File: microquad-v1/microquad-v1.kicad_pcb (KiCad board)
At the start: 2 copper layers, 53.3 x 53.3 mm, 79 parts, among them J1 USB_microB_2040002-1, M1 Motor_DC, M2 Motor_DC, M3 Motor_DC, M4 Motor_DC, M5 Motor_DC, M6 Motor_DC, Q1 Q_NMOS_GSD, Q2 Q_NMOS_GSD, Q3 Q_NMOS_GSD, Q4 Q_NMOS_GSD, Q5 Q_NMOS_GSD, Q6 Q_NMOS_GSD, SW1 SERIAL, SW2 POWER, SW3 RESET, U1 ATMEGA328PB, U2 MCP1703A-3302_SOT23, U3 FT230XS, U4 MCP73812T, U5 MAX6333UR18D3

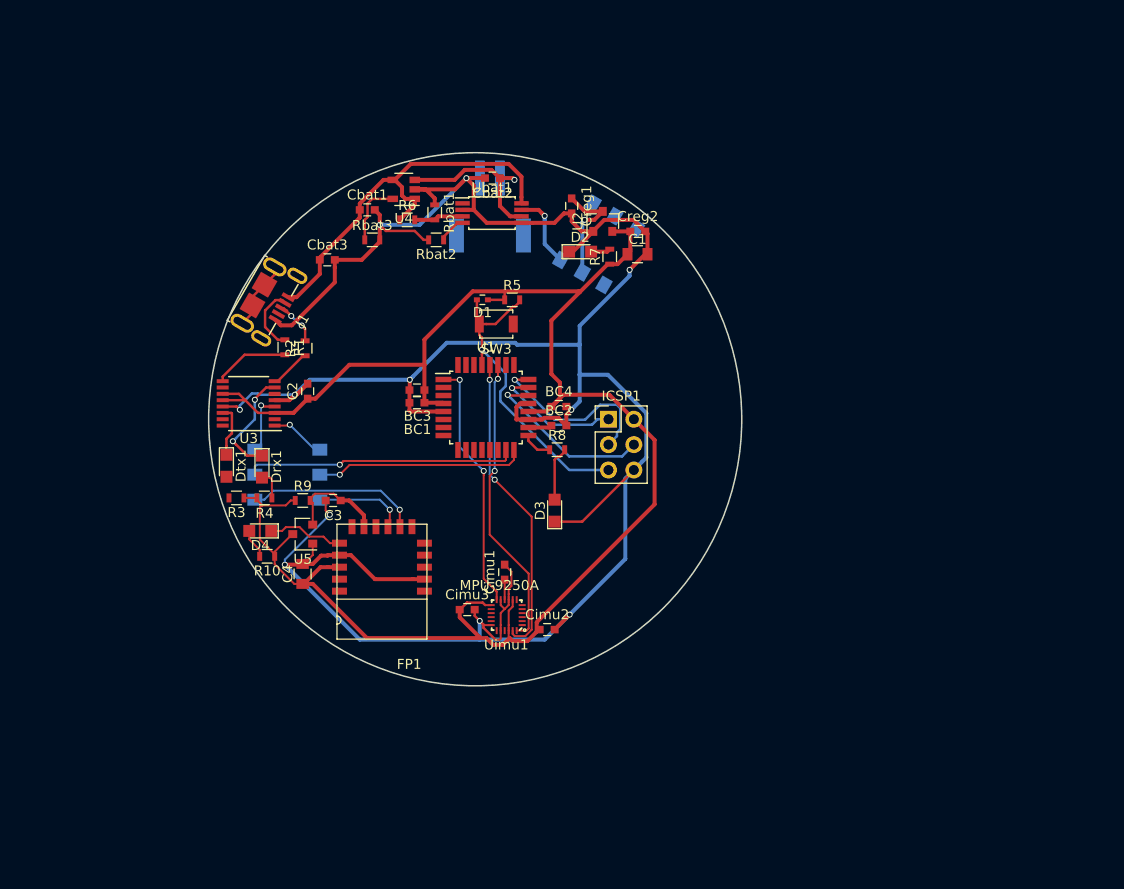
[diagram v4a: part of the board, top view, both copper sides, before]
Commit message: Added ground pour
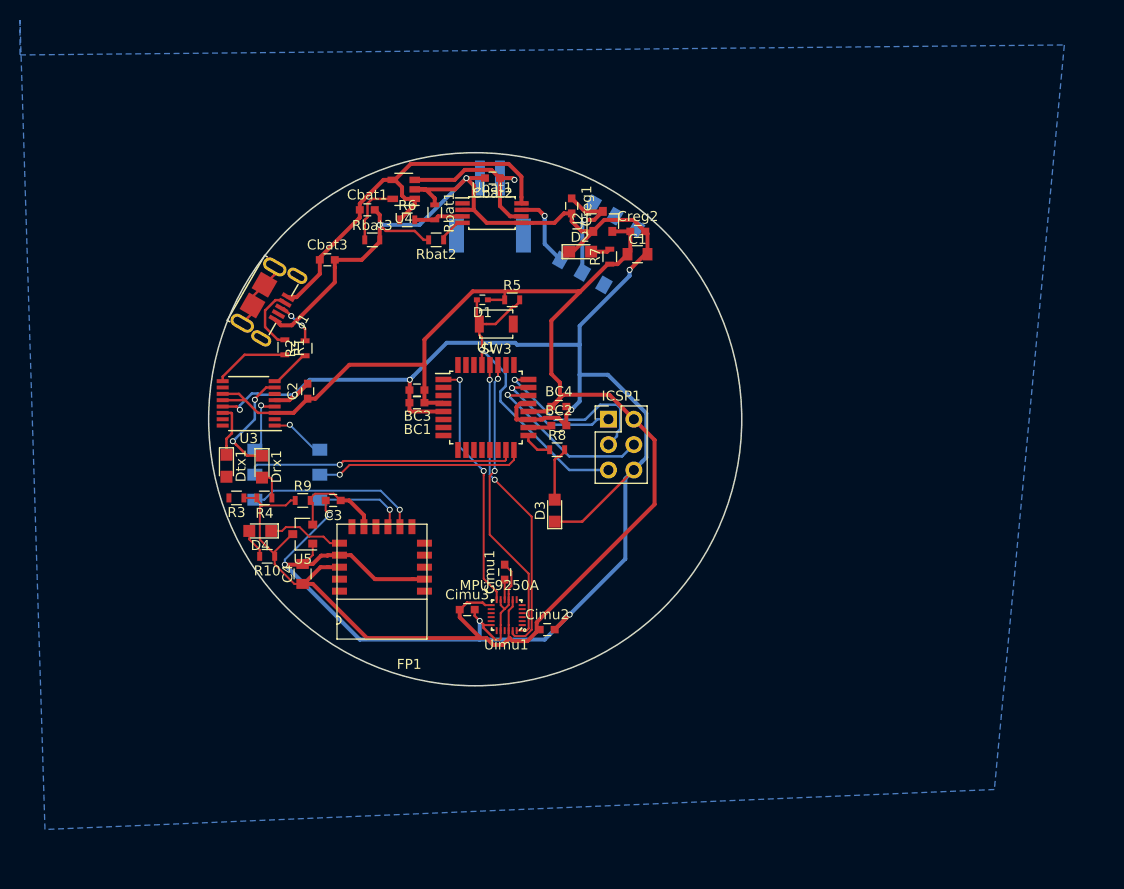
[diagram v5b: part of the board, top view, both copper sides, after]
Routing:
- added copper zone on B.Cu, net GND
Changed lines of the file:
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@@
   (segment (start 149.781073 104.775) (end 149.730288 104.825785) (width 0.25) (layer F.Cu) (net 31))
   (segment (start 150 104) (end 151.35 104) (width 0.25) (layer F.Cu) (net 32))
+  (segment (start 160.234999 109.640001) (end 160.234999 109.265001) (width 0.25) (layer B.Cu) (net 32))
+  (segment (start 159.385 110.49) (end 160.234999 109.640001) (width 0.25) (layer B.Cu) (net 32))
+  (segment (start 160.560001 106.839999) (end 160.220002 106.5) (width 0.25) (layer B.Cu) (net 32))
+  (segment (start 160.560001 108.939999) (end 160.560001 106.839999) (width 0.25) (layer B.Cu) (net 32))
+  (segment (start 160.234999 109.265001) (end 160.560001 108.939999) (width 0.25) (layer B.Cu) (net 32))
+  (segment (start 158.549998 106.5) (end 157.049998 108) (width 0.25) (layer B.Cu) (net 32))
+  (segment (start 160.220002 106.5) (end 158.549998 106.5) (width 0.25) (layer B.Cu) (net 32))
+  (via (at 150 104) (size 0.6) (drill 0.4) (layers F.Cu B.Cu) (net 32))
+  (segment (start 154 108) (end 150 104) (width 0.25) (layer B.Cu) (net 32))
+  (segment (start 157.049998 108) (end 154 108) (width 0.25) (layer B.Cu) (net 32))
   (segment (start 151.35 104) (end 151.375 103.975) (width 0.25) (layer F.Cu) (net 32))
-  (segment (start 157.049998 108) (end 154 108) (width 0.25) (layer B.Cu) (net 32))
-  (segment (start 154 108) (end 150 104) (width 0.25) (layer B.Cu) (net 32))
-  (via (at 150 104) (size 0.6) (drill 0.4) (layers F.Cu B.Cu) (net 32))
-  (segment (start 160.220002 106.5) (end 158.549998 106.5) (width 0.25) (layer B.Cu) (net 32))
-  (segment (start 158.549998 106.5) (end 157.049998 108) (width 0.25) (layer B.Cu) (net 32))
-  (segment (start 160.234999 109.265001) (end 160.560001 108.939999) (width 0.25) (layer B.Cu) (net 32))
-  (segment (start 160.560001 108.939999) (end 160.560001 106.839999) (width 0.25) (layer B.Cu) (net 32))
-  (segment (start 160.560001 106.839999) (end 160.220002 106.5) (width 0.25) (layer B.Cu) (net 32))
-  (segment (start 159.385 110.49) (end 160.234999 109.640001) (width 0.25) (layer B.Cu) (net 32))
-  (segment (start 160.234999 109.640001) (end 160.234999 109.265001) (width 0.25) (layer B.Cu) (net 32))
   (segment (start 161.925 110.49) (end 160.749999 111.665001) (width 0.25) (layer B.Cu) (net 33))
   (segment (start 149.364143 105.575) (end 149.296792 105.507649) (width 0.25) (layer F.Cu) (net 33))
@@
   (segment (start 151.700012 129.014269) (end 151.700012 127.799988) (width 0.2) (layer F.Cu) (net 55))
   (segment (start 149.8 129.1) (end 149.8 129.442881) (width 0.2) (layer F.Cu) (net 55))
+  (zone (net 1) (net_name GND) (layer B.Cu) (hatch edge 0.508)
+    (connect_pads (clearance 0.508))
+    (min_thickness 0.254)
+    (fill yes (arc_segments 16) (thermal_gap 0.508) (thermal_bridge_width 0.508))
+    (polygon
+      (pts
+        (xy 100.5 71.5) (xy 205 70.5) (xy 198 145) (xy 103 149) (xy 100.5 68)
+      )
+    )
+  )
 )

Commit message: Made a pretty array of motors
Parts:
- added C10: 10uF, Capacitors_SMD:C_0805, F.Cu at (225.3, 72.6)
- added C10: 10uF, Capacitors_SMD:C_0805, F.Cu at (250.7, 68.8)
- added C10: 10uF, Capacitors_SMD:C_0805, F.Cu at (266.7, 88.9)
- added C10: 10uF, Capacitors_SMD:C_0805, F.Cu at (257.3, 112.8)
- added C10: 10uF, Capacitors_SMD:C_0805, F.Cu at (231.9, 116.6)
- added D15: BAS521LP-7, Diodes_SMD:D_SOD-123F, F.Cu at (226.7, 67.4)
- added D15: BAS521LP-7, Diodes_SMD:D_SOD-123F, F.Cu at (255.9, 67.4)
- added D15: BAS521LP-7, Diodes_SMD:D_SOD-123F, F.Cu at (270.5, 92.7)
- added D15: BAS521LP-7, Diodes_SMD:D_SOD-123F, F.Cu at (255.9, 118.0)
- added D15: BAS521LP-7, Diodes_SMD:D_SOD-123F, F.Cu at (226.7, 118.0)
- added D16: DNP, Diodes_SMD:D_2114, F.Cu at (230.3, 71.2)
- added D16: DNP, Diodes_SMD:D_2114, F.Cu at (254.5, 72.4)
- added D16: DNP, Diodes_SMD:D_2114, F.Cu at (265.4, 94.0)
- added D16: DNP, Diodes_SMD:D_2114, F.Cu at (252.3, 114.2)
- added D16: DNP, Diodes_SMD:D_2114, F.Cu at (228.1, 113.0)
- added M6: Motor_DC, motor:quad_motor_v1, F.Cu at (223.5, 61.9)
- added M6: Motor_DC, motor:quad_motor_v1, F.Cu at (259.1, 61.9)
- added M6: Motor_DC, motor:quad_motor_v1, F.Cu at (276.9, 92.7)
- added M6: Motor_DC, motor:quad_motor_v1, F.Cu at (259.1, 123.5)
- added M6: Motor_DC, motor:quad_motor_v1, F.Cu at (223.5, 123.5)
- added Q6: Q_NMOS_GSD, TO_SOT_Packages_SMD:SOT-23, F.Cu at (231.8, 76.2)
- added Q6: Q_NMOS_GSD, TO_SOT_Packages_SMD:SOT-23, F.Cu at (250.8, 76.2)
- added Q6: Q_NMOS_GSD, TO_SOT_Packages_SMD:SOT-23, F.Cu at (260.4, 92.7)
- added Q6: Q_NMOS_GSD, TO_SOT_Packages_SMD:SOT-23, F.Cu at (250.8, 109.2)
- added Q6: Q_NMOS_GSD, TO_SOT_Packages_SMD:SOT-23, F.Cu at (231.8, 109.2)
- moved D15 105.0 mm to (212.1, 92.7), turned to 90 degrees
- moved M6 102.3 mm to (205.7, 92.7), turned to 90 degrees
- moved C10 101.5 mm to (215.9, 96.5)
- moved D16 100.3 mm to (217.2, 91.4), turned to 270 degrees
- moved Q6 98.5 mm to (222.2, 92.7)

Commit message: Fixed motor component labels and reimported netlist
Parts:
- removed the C5 at (135.0, 203.2)
- removed the C6 at (148.8, 227.6)
- removed the C7 at (186.3, 197.5)
- removed the C8 at (224.4, 223.6)
- removed the C9 at (186.7, 223.0)
- removed the D10 at (188.2, 191.2)
- removed the D11 at (217.3, 223.5)
- removed the D12 at (226.3, 217.3)
- removed the D13 at (179.7, 222.9)
- removed the D14 at (188.6, 216.6)
- removed the D5 at (128.0, 203.6)
- removed the D6 at (143.4, 198.2)
- removed the D7 at (141.7, 227.5)
- removed the D8 at (150.6, 221.2)
- removed the D9 at (179.2, 197.4)
- removed the M1 at (132.1, 194.1)
- removed the M2 at (130.1, 224.9)
- removed the M3 at (167.6, 194.8)
- removed the M4 at (205.7, 220.9)
- removed the M5 at (168.0, 220.3)
- removed the Q1 at (144.6, 191.0)
- removed the Q2 at (141.8, 221.0)
- removed the Q3 at (179.3, 191.0)
- removed the Q4 at (217.4, 217.1)
- removed the Q5 at (179.7, 216.4)
- renumbered C10 to C5, C10 to C6, C10 to C7, C10 to C8, C10 to C9, D16 to D10, D15 to D11, D16 to D12, D15 to D13, D16 to D14, D15 to D5, D16 to D6, D15 to D7, D16 to D8, D15 to D9, M6 to M1, M6 to M2, M6 to M3, M6 to M4, M6 to M5, Q6 to Q1, Q6 to Q2, Q6 to Q3, Q6 to Q4, Q6 to Q5
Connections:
- C5 pad 2: /Motor6/VBAT -> /Motor1/VBAT
- C6 pad 2: /Motor6/VBAT -> /Motor2/VBAT
- C7 pad 2: /Motor6/VBAT -> /Motor3/VBAT
- C8 pad 2: /Motor6/VBAT -> /Motor4/VBAT
- C9 pad 2: /Motor6/VBAT -> /Motor5/VBAT
- D10 pad 1: Net-(D15-Pad2) -> Net-(D10-Pad1)
- D11 pad 1: /Motor6/VBAT -> /Motor4/VBAT
- D11 pad 2: Net-(D15-Pad2) -> Net-(D11-Pad2)
- D12 pad 1: Net-(D15-Pad2) -> Net-(D11-Pad2)
- D13 pad 1: /Motor6/VBAT -> /Motor5/VBAT
- D13 pad 2: Net-(D15-Pad2) -> Net-(D13-Pad2)
- D14 pad 1: Net-(D15-Pad2) -> Net-(D13-Pad2)
- D5 pad 1: /Motor6/VBAT -> /Motor1/VBAT
- D5 pad 2: Net-(D15-Pad2) -> Net-(D5-Pad2)
- D6 pad 1: Net-(D15-Pad2) -> Net-(D5-Pad2)
- D7 pad 1: /Motor6/VBAT -> /Motor2/VBAT
- D7 pad 2: Net-(D15-Pad2) -> Net-(D7-Pad2)
- D8 pad 1: Net-(D15-Pad2) -> Net-(D7-Pad2)
- D9 pad 1: /Motor6/VBAT -> /Motor3/VBAT
- D9 pad 2: Net-(D15-Pad2) -> Net-(D10-Pad1)
- FP1 pad 1: (no net) -> Net-(FP1-Pad1)
- FP1 pad 11: (no net) -> Net-(FP1-Pad11)
- FP1 pad 15: (no net) -> Net-(FP1-Pad15)
- FP1 pad 16: (no net) -> Net-(FP1-Pad16)
- FP1 pad 3: (no net) -> Net-(FP1-Pad3)
- FP1 pad 4: (no net) -> Net-(FP1-Pad4)
- FP1 pad 5: (no net) -> Net-(FP1-Pad5)
- FP1 pad 6: (no net) -> Net-(FP1-Pad6)
- FP1 pad 9: (no net) -> Net-(FP1-Pad9)
- J1 pad 4: (no net) -> Net-(J1-Pad4)
- M1 pad 1: /Motor6/VBAT -> /Motor1/VBAT
- M1 pad 2: Net-(D15-Pad2) -> Net-(D5-Pad2)
- M2 pad 1: /Motor6/VBAT -> /Motor2/VBAT
- M2 pad 2: Net-(D15-Pad2) -> Net-(D7-Pad2)
- M3 pad 1: /Motor6/VBAT -> /Motor3/VBAT
- M3 pad 2: Net-(D15-Pad2) -> Net-(D10-Pad1)
- M4 pad 1: /Motor6/VBAT -> /Motor4/VBAT
- M4 pad 2: Net-(D15-Pad2) -> Net-(D11-Pad2)
- M5 pad 1: /Motor6/VBAT -> /Motor5/VBAT
- M5 pad 2: Net-(D15-Pad2) -> Net-(D13-Pad2)
- Q1 pad 1: /Motor6/ENABLE -> /Motor1/ENABLE
- Q1 pad 3: Net-(D15-Pad2) -> Net-(D5-Pad2)
- Q2 pad 1: /Motor6/ENABLE -> /Motor2/ENABLE
- Q2 pad 3: Net-(D15-Pad2) -> Net-(D7-Pad2)
- Q3 pad 1: /Motor6/ENABLE -> /Motor3/ENABLE
- Q3 pad 3: Net-(D15-Pad2) -> Net-(D10-Pad1)
- Q4 pad 1: /Motor6/ENABLE -> /Motor4/ENABLE
- Q4 pad 3: Net-(D15-Pad2) -> Net-(D11-Pad2)
- Q5 pad 1: /Motor6/ENABLE -> /Motor5/ENABLE
- Q5 pad 3: Net-(D15-Pad2) -> Net-(D13-Pad2)
- SW2 pad 1: (no net) -> Net-(SW2-Pad1)
- U1 pad 11: (no net) -> Net-(U1-Pad11)
- U1 pad 12: (no net) -> Net-(U1-Pad12)
- U1 pad 2: (no net) -> Net-(U1-Pad2)
- U1 pad 25: (no net) -> Net-(U1-Pad25)
- U1 pad 26: (no net) -> Net-(U1-Pad26)
- U1 pad 3: (no net) -> Net-(U1-Pad3)
- U1 pad 6: (no net) -> Net-(U1-Pad6)
- U1 pad 7: (no net) -> Net-(U1-Pad7)
- U1 pad 8: (no net) -> Net-(U1-Pad8)
- U1 pad 9: (no net) -> Net-(U1-Pad9)
- U3 pad 10: (no net) -> Net-(U3-Pad10)
- U3 pad 15: (no net) -> Net-(U3-Pad15)
- U3 pad 16: (no net) -> Net-(U3-Pad16)
- U3 pad 2: (no net) -> Net-(U3-Pad2)
- U3 pad 6: (no net) -> Net-(U3-Pad6)
- Ubat1 pad 1: (no net) -> Net-(Ubat1-Pad1)
- Uimu1 pad 14: (no net) -> Net-(Uimu1-Pad14)
- Uimu1 pad 15: (no net) -> Net-(Uimu1-Pad15)
- Uimu1 pad 16: (no net) -> Net-(Uimu1-Pad16)
- Uimu1 pad 17: (no net) -> Net-(Uimu1-Pad17)
- Uimu1 pad 19: (no net) -> Net-(Uimu1-Pad19)
- Uimu1 pad 2: (no net) -> Net-(Uimu1-Pad2)
- Uimu1 pad 21: (no net) -> Net-(Uimu1-Pad21)
- Uimu1 pad 3: (no net) -> Net-(Uimu1-Pad3)
- Uimu1 pad 4: (no net) -> Net-(Uimu1-Pad4)
- Uimu1 pad 5: (no net) -> Net-(Uimu1-Pad5)
- Uimu1 pad 6: (no net) -> Net-(Uimu1-Pad6)
- Uimu1 pad 7: (no net) -> Net-(Uimu1-Pad7)
